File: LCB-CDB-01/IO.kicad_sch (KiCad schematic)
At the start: 64 parts, among them J100 01x02, J101 01x02, J102 01x02, J103 01x02, J104 01x02, J105 01x02, J106 01x02, J107 01x02, J130 01x02, J131 01x02, J132 01x02, J133 01x02, J134 01x02, J135 01x02, J136 01x02, J137 01x02, J138 01x02, J139 01x02, J140 01x02, J141 01x02, J150 01x02, J151 01x02, J152 01x02, J153 01x02, J154 01x02, J155 01x02, J156 01x02, J157 01x02, J158 01x02, J159 01x02, J160 01x02, J161 01x02, SW1 SW_Push, SW2 SW_Push, SW3 SW_Push, SW4 SW_Push, U100 ST_6CH_CMOS_SOIC14_MC74HC14ADG, U101 ST_6CH_CMOS_SOIC14_MC74HC14ADG

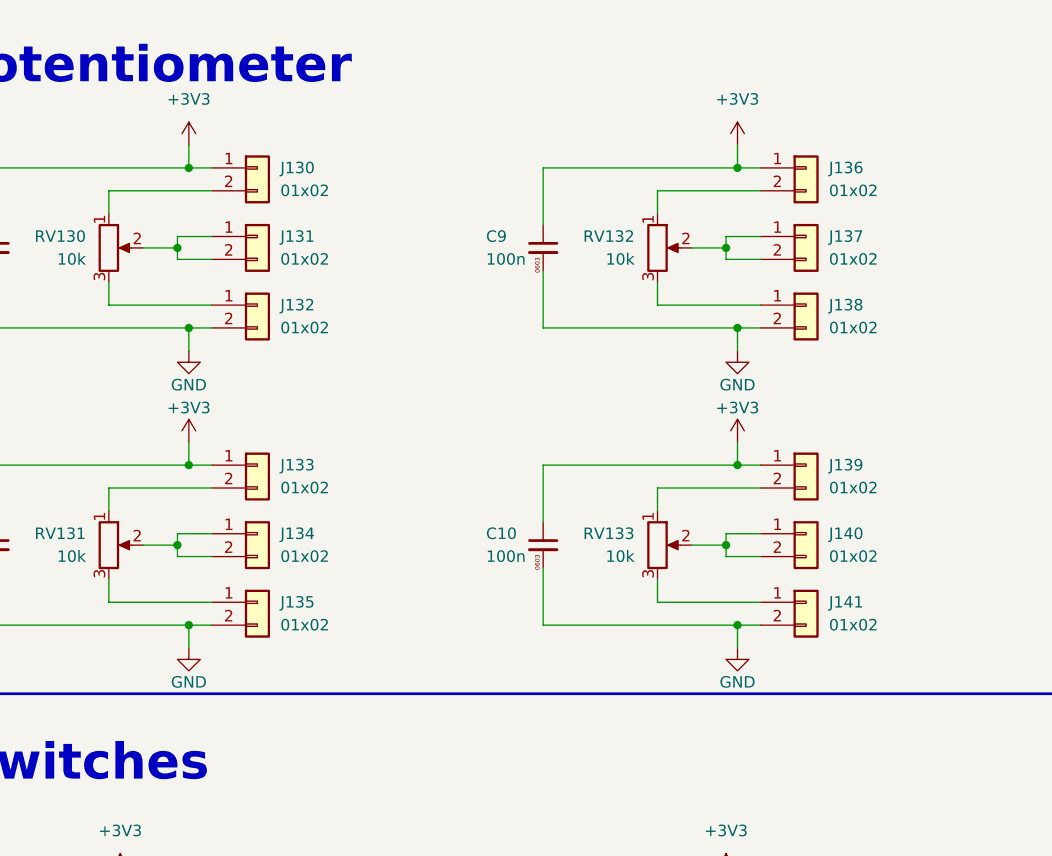
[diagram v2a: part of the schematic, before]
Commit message: update: Issue fix - 3V supply for potentiometers
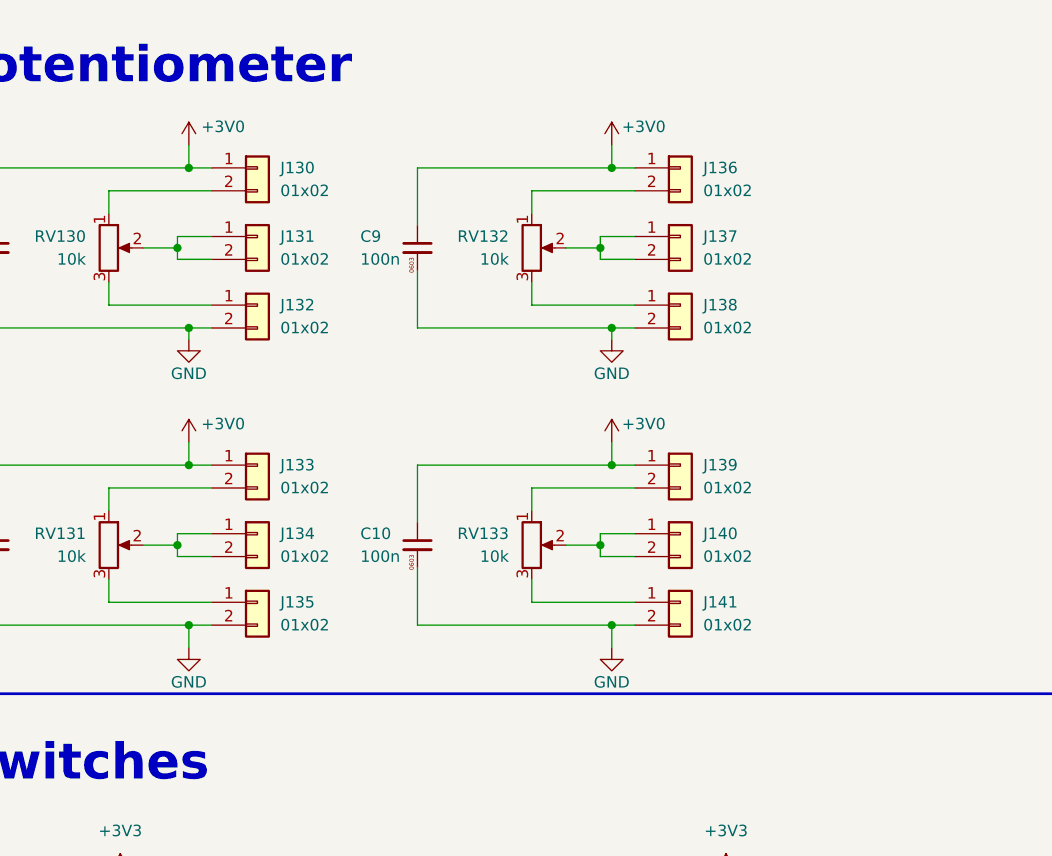
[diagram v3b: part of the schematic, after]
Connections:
- net +3V3: no longer C10.1, C7.1, C8.1, C9.1, J130.1 (Pin_1), J133.1 (Pin_1), J136.1 (Pin_1), J139.1 (Pin_1)
- new net +3V0: C10.1, C7.1, C8.1, C9.1, J130.1 (Pin_1), J133.1 (Pin_1), J136.1 (Pin_1), J139.1 (Pin_1)
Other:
- moved on the sheet: C10, C9, J136, J137, J138, J139, J140, J141, RV132, RV133

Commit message: update symbols without simulation models
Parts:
- J100, J101, J102, J103, J104, J105, J106, J107, J130, J131, J132, J133, J134, J135, J136, J137, J138, J139, J140, J141, J150, J151, J152, J153, J154, J155, J156, J157, J158, J159, J160, J161: Mouser No. 855-M20-9990245 -> (none)
- RV130, RV131, RV132, RV133: Mouser No. 652-PTV09A-4020FB103 -> (none)
- S100, S101, S103, S104: Mfr. No 2MS1T1B1M2QES -> (none); Mouser No 118-2MS1T1B1M2QES -> (none)
- SW1, SW2, SW3, SW4: Mouser No. 179-TS046643BK160SMT -> (none)
- U100, U101: Mouser No. 863-MC74HC14ADG -> (none)
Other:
- title: LCB-CBD-01: Dock -> LCB-CDB-01: Dock Board
